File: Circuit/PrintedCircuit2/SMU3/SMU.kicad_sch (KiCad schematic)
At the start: 21 parts, among them J1 Conn_Coaxial, J2 Conn_Coaxial, SW1 SW_SPDT, SW2 SW_SPDT, U1 TPS65131_kit, U2 MCP1501-20xCH, U3 MCP4922

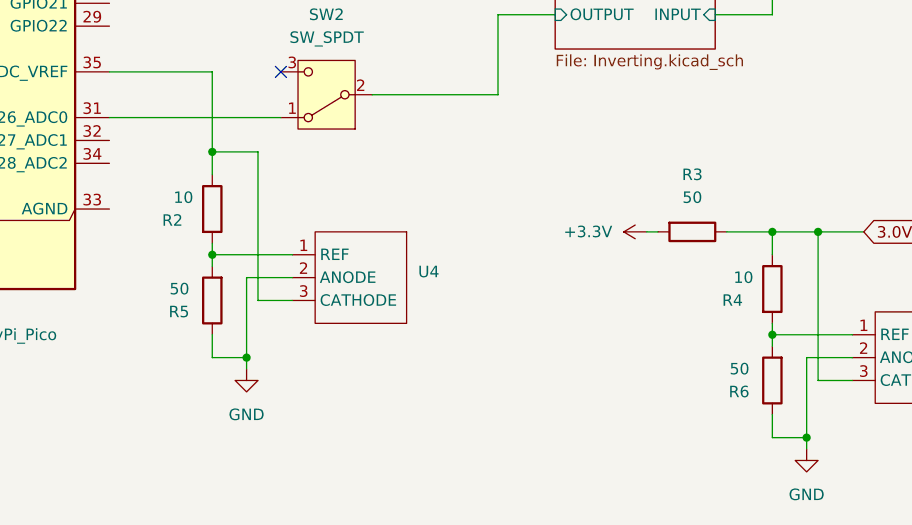
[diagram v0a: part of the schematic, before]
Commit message: 3Dモデルを更新
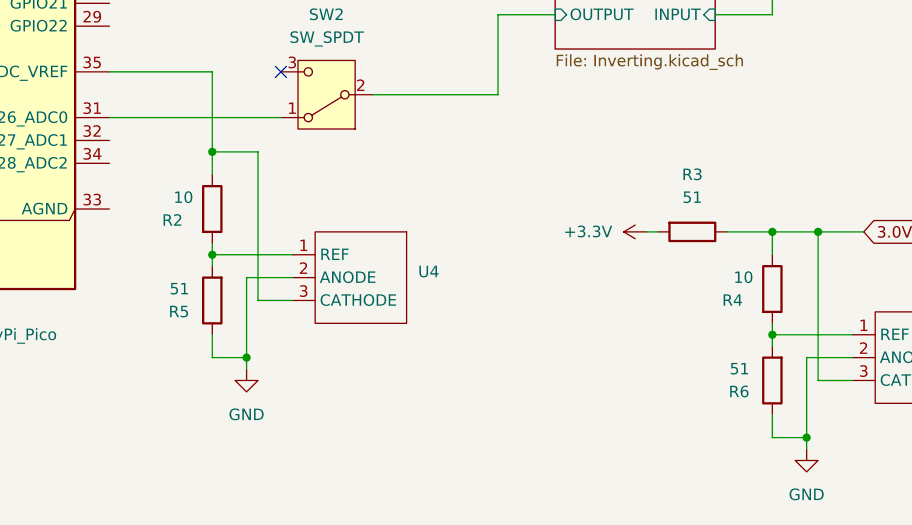
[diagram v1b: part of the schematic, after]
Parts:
- R3, R5, R6: value 50 -> 51
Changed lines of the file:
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@@
 			)
 		)
-		(property "Value" "50"
+		(property "Value" "51"
 			(at 83.82 153.6701 0)
 			(effects
@@
 			)
 		)
-		(property "Value" "50"
+		(property "Value" "51"
 			(at 139.7 143.51 90)
 			(effects
@@
 			)
 		)
-		(property "Value" "50"
+		(property "Value" "51"
 			(at 146.05 162.5601 0)
 			(effects

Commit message: 更新
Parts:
- R3, R6: value 51 -> 51Ω
- R4: value 10 -> 10Ω
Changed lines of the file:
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@@
 			)
 		)
-		(property "Value" "51"
+		(property "Value" "51Ω"
 			(at 139.7 143.51 90)
 			(effects
@@
 		(on_board yes)
 		(dnp no)
-		(fields_autoplaced yes)
 		(property "Reference" "R6"
-			(at 146.05 165.1001 0)
-			(effects
-				(font
-					(size 1.27 1.27)
-				)
-				(justify left)
-			)
-		)
-		(property "Value" "51"
-			(at 146.05 162.5601 0)
-			(effects
-				(font
-					(size 1.27 1.27)
-				)
-				(justify left)
+			(at 142.494 162.306 0)
+			(effects
+				(font
+					(size 1.27 1.27)
+				)
+				(justify right)
+			)
+		)
+		(property "Value" "51Ω"
+			(at 142.494 164.846 0)
+			(effects
+				(font
+					(size 1.27 1.27)
+				)
+				(justify right)
 			)
 		)
@@
 			)
 		)
-		(property "Value" "10"
-			(at 144.272 152.4 0)
-			(effects
-				(font
+		(property "Value" "10Ω"
+			(at 142.748 152.4 0)
+			(effects
+				(font

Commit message: β0.0.3
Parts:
- added R6: 51, Resistor_SMD:R_0603_1608Metric, symbol Device:R
- R2: value 10 -> 1k; footprint Resistor_SMD:R_0603_1608Metric_Pad0.98x0.95mm_HandSolder -> Resistor_SMD:R_0603_1608Metric
- R3: value 51Ω -> 51; footprint Resistor_SMD:R_0603_1608Metric_Pad0.98x0.95mm_HandSolder -> Resistor_SMD:R_0603_1608Metric
- R4: value 10Ω -> 1k; footprint Resistor_SMD:R_0603_1608Metric_Pad0.98x0.95mm_HandSolder -> Resistor_SMD:R_0603_1608Metric
- R5: value 51 -> 5.1k; footprint Resistor_SMD:R_0603_1608Metric_Pad0.98x0.95mm_HandSolder -> Resistor_SMD:R_0603_1608Metric
- R7: renamed from R6; value 51Ω -> 5.1k; footprint Resistor_SMD:R_0603_1608Metric_Pad0.98x0.95mm_HandSolder -> Resistor_SMD:R_0603_1608Metric
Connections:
- net +3.3V: now also R6.2
- net at A1.35 (ADC_VREF), R2.1, U4.3 (CATHODE): now also R6.1
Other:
- note removed: "SHDNの接続ミス PCB未修正"
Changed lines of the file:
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@@
 		)
 	)
-	(text "SHDNの接続ミス\nPCB未修正"
-		(exclude_from_sim no)
-		(at 94.234 55.626 0)
-		(effects
-			(font
-				(size 1.27 1.27)
-			)
-		)
+	(junction
+		(at 80.01 129.54)
+		(diameter 0)
+		(color 0 0 0 0)
 	)
 	(junction
@@
 	(wire
 		(pts
+			(xy 80.01 158.75) (xy 80.01 129.54)
+		)
+		(stroke
+			(width 0)
+			(type default)
+		)
+	)
+	(wire
+		(pts
 			(xy 223.52 113.03) (xy 231.14 113.03)
 		)
@@
 	(wire
 		(pts
-			(xy 74.93 129.54) (xy 86.36 129.54)
+			(xy 74.93 129.54) (xy 80.01 129.54)
 		)
 		(stroke
@@
 	(wire
 		(pts
+			(xy 80.01 167.64) (xy 80.01 166.37)
+		)
+		(stroke
+			(width 0)
+			(type default)
+		)
+	)
+	(wire
+		(pts
+			(xy 80.01 129.54) (xy 86.36 129.54)
+		)
+		(stroke
+			(width 0)
+			(type default)
+		)
+	)
+	(wire
+		(pts
 			(xy 190.5 104.14) (xy 200.66 104.14)
 		)
@@
 		(dnp no)
 		(fields_autoplaced yes)
-		(property "Reference" "#PWR015"
+		(property "Reference" "#PWR016"
 			(at 152.4 177.8 0)
 			(effects
@@
 			(project "SMU"
 				(path "/736408a4-d995-4f38-bf98-0d13d4319ec4"
-					(reference "#PWR015")
+					(reference "#PWR016")
 					(unit 1)
 				)
@@
 	)
 	(symbol
+		(lib_id "power:+3.3V")
+		(at 80.01 167.64 180)
+		(unit 1)
+		(exclude_from_sim no)
+		(in_bom yes)
+		(on_board yes)
+		(dnp no)
+		(fields_autoplaced yes)
+		(property "Reference" "#PWR015"
+			(at 80.01 163.83 0)
+			(effects
+				(font
+					(size 1.27 1.27)
+				)
+				(hide yes)
+			)
+		)
+		(property "Value" "+3.3V"
+			(at 80.0099 171.45 90)
+			(effects
+				(font
+					(size 1.27 1.27)
+				)
+				(justify left)
+			)
+		)
+		(property "Footprint" ""
+			(at 80.01 167.64 0)
+			(effects
+				(font
+					(size 1.27 1.27)
+				)
+				(hide yes)
+			)
+		)
+		(property "Datasheet" ""
+			(at 80.01 167.64 0)
+			(effects
+				(font
+					(size 1.27 1.27)
+				)
+				(hide yes)
+			)
+		)
+		(property "Description" "Power symbol creates a global label with name \"+3.3V\""
+			(at 80.01 167.64 0)
+			(effects
+				(font
+					(size 1.27 1.27)
+				)
+				(hide yes)
+			)
+		)
+		(pin "1"
+		)
+		(instances
+			(project "SMU"
+				(path "/736408a4-d995-4f38-bf98-0d13d4319ec4"
+					(reference "#PWR015")
+					(unit 1)
+				)
+			)
+		)
+	)
+	(symbol
 		(lib_id "power:-12V")
 		(at 80.01 41.91 270)
@@
 			)
 		)
-		(property "Value" "51"
+		(property "Value" "5.1k"
 			(at 83.82 153.6701 0)
 			(effects
@@
 			)
 		)
-		(property "Footprint" "Resistor_SMD:R_0603_1608Metric_Pad0.98x0.95mm_HandSolder"
+		(property "Footprint" "Resistor_SMD:R_0603_1608Metric"
 			(at 88.138 154.94 90)
 			(effects
@@
 			)
 		)
-		(property "Value" "51Ω"
+		(property "Value" "51"
 			(at 139.7 143.51 90)
 			(effects
@@
 			)
 		)
-		(property "Footprint" "Resistor_SMD:R_0603_1608Metric_Pad0.98x0.95mm_HandSolder"
+		(property "Footprint" "Resistor_SMD:R_0603_1608Metric"
 			(at 139.7 145.542 90)
 			(effects
@@
 			)
 		)
-		(property "Value" "10"
+		(property "Value" "1k"
 			(at 82.042 143.51 0)
 			(effects
@@
 			)
 		)
-		(property "Footprint" "Resistor_SMD:R_0603_1608Metric_Pad0.98x0.95mm_HandSolder"
+		(property "Footprint" "Resistor_SMD:R_0603_1608Metric"
 			(at 84.582 144.78 90)
 			(effects
@@
 	)
 	(symbol
+		(lib_id "Device:R")
+		(at 80.01 162.56 0)
+		(unit 1)
+		(exclude_from_sim no)
+		(in_bom yes)
+		(on_board yes)
+		(dnp no)
+		(fields_autoplaced yes)
+		(property "Reference" "R6"
+			(at 73.66 162.56 90)
+			(effects
+				(font
+					(size 1.27 1.27)
+				)
+			)
+		)
+		(property "Value" "51"
+			(at 76.2 162.56 90)
+			(effects
+				(font
+					(size 1.27 1.27)
+				)
+			)
+		)
+		(property "Footprint" "Resistor_SMD:R_0603_1608Metric"
+			(at 78.232 162.56 90)
+			(effects
+				(font
+					(size 1.27 1.27)
+				)
+				(hide yes)
+			)
+		)
+		(property "Datasheet" "~"
+			(at 80.01 162.56 0)
+			(effects
+				(font
+					(size 1.27 1.27)
+				)
+				(hide yes)
+			)
+		)
+		(property "Description" "Resistor"
+			(at 80.01 162.56 0)
+			(effects
+				(font
+					(size 1.27 1.27)
+				)
+				(hide yes)
+			)
+		)
+		(property "Sim.Device" "R"
+			(at 80.01 162.56 0)
+			(effects
+				(font
+					(size 1.27 1.27)
+				)
+				(hide yes)
+			)
+		)
+		(property "Sim.Type" "="
+			(at 80.01 162.56 0)
+			(effects
+				(font
+					(size 1.27 1.27)
+				)
+				(hide yes)
+			)
+		)
+		(property "Sim.Params" "r=30k"
+			(at 80.01 162.56 0)
+			(effects
+				(font
+					(size 1.27 1.27)
+				)
+				(hide yes)
+			)
+		)
+		(property "Sim.Pins" "1=+ 2=-"
+			(at 80.01 162.56 0)
+			(effects
+				(font
+					(size 1.27 1.27)
+				)
+				(hide yes)
+			)
+		)
+		(pin "2"
+		)
+		(pin "1"
+		)
+		(instances
+			(project "SMU"
+				(path "/736408a4-d995-4f38-bf98-0d13d4319ec4"
+					(reference "R6")
+					(unit 1)
+				)
+			)
+		)
+	)
+	(symbol
 		(lib_id "power:GND")
 		(at 111.76 62.23 0)
@@
 		(on_board yes)
 		(dnp no)
-		(property "Reference" "R6"
+		(property "Reference" "R7"
 			(at 142.494 162.306 0)
 			(effects
@@
 			)
 		)
-		(property "Value" "51Ω"
+		(property "Value" "5.1k"
 			(at 142.494 164.846 0)
 			(effects
@@
 			)
 		)
-		(property "Footprint" "Resistor_SMD:R_0603_1608Metric_Pad0.98x0.95mm_HandSolder"
+		(property "Footprint" "Resistor_SMD:R_0603_1608Metric"
 			(at 150.368 163.83 90)
 			(effects
@@
 			(project "SMU"
 				(path "/736408a4-d995-4f38-bf98-0d13d4319ec4"
-					(reference "R6")
+					(reference "R7")
 					(unit 1)
 				)
@@
 			)
 		)
-		(property "Value" "10Ω"
+		(property "Value" "1k"
 			(at 142.748 152.4 0)
 			(effects
@@
 			)
 		)
-		(property "Footprint" "Resistor_SMD:R_0603_1608Metric_Pad0.98x0.95mm_HandSolder"
+		(property "Footprint" "Resistor_SMD:R_0603_1608Metric"
 			(at 146.812 153.67 90)
 			(effects

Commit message: 保護回路を変更
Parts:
- renumbered C5 to C4, C4 to C5, R6 to R1, R5 to R3, R1 to R4, R3 to R5, R4 to R6, SW2 to SW1, SW1 to SW2, U4 to U2, U2 to U3, U3 to U4
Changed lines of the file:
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@@
 		(dnp no)
 		(fields_autoplaced yes)
-		(property "Reference" "#PWR09"
+		(property "Reference" "#PWR03"
 			(at 57.15 85.09 0)
 			(effects
@@
 			(project ""
 				(path "/736408a4-d995-4f38-bf98-0d13d4319ec4"
-					(reference "#PWR09")
+					(reference "#PWR03")
 					(unit 1)
 				)
@@
 		(dnp no)
 		(fields_autoplaced yes)
-		(property "Reference" "#PWR03"
+		(property "Reference" "#PWR09"
 			(at 99.06 26.67 0)
 			(effects
@@
 			(project "SMU"
 				(path "/736408a4-d995-4f38-bf98-0d13d4319ec4"
-					(reference "#PWR03")
+					(reference "#PWR09")
 					(unit 1)
 				)
@@
 		(dnp no)
 		(fields_autoplaced yes)
-		(property "Reference" "#PWR014"
+		(property "Reference" "#PWR02"
 			(at 52.07 171.45 0)
 			(effects
@@
 			(project ""
 				(path "/736408a4-d995-4f38-bf98-0d13d4319ec4"
-					(reference "#PWR014")
+					(reference "#PWR02")
 					(unit 1)
 				)
@@
 		(dnp no)
 		(fields_autoplaced yes)
-		(property "Reference" "#PWR010"
+		(property "Reference" "#PWR014"
 			(at 118.11 101.6 0)
 			(effects
@@
 			(project "SMU"
 				(path "/736408a4-d995-4f38-bf98-0d13d4319ec4"
-					(reference "#PWR010")
+					(reference "#PWR014")
 					(unit 1)
 				)
@@
 		(dnp no)
 		(fields_autoplaced yes)
-		(property "Reference" "SW2"
+		(property "Reference" "SW1"
 			(at 99.06 123.19 0)
 			(effects
@@
 			(project "SMU"
 				(path "/736408a4-d995-4f38-bf98-0d13d4319ec4"
-					(reference "SW2")
+					(reference "SW1")
 					(unit 1)
 				)
@@
 		(dnp no)
 		(fields_autoplaced yes)
-		(property "Reference" "#PWR012"
+		(property "Reference" "#PWR015"
 			(at 138.43 147.32 0)
 			(effects
@@
 			(project "SMU"
 				(path "/736408a4-d995-4f38-bf98-0d13d4319ec4"
-					(reference "#PWR012")
+					(reference "#PWR015")
 					(unit 1)
 				)
@@
 		(dnp no)
 		(fields_autoplaced yes)
-		(property "Reference" "#PWR01"
+		(property "Reference" "#PWR07"
 			(at 77.47 21.59 0)
 			(effects
@@
 			(project ""
 				(path "/736408a4-d995-4f38-bf98-0d13d4319ec4"
-					(reference "#PWR01")
+					(reference "#PWR07")
 					(unit 1)
 				)
@@
 		(dnp no)
 		(fields_autoplaced yes)
-		(property "Reference" "C5"
+		(property "Reference" "C4"
 			(at 107.95 109.2199 0)
 			(effects
@@
 			(project "SMU"
 				(path "/736408a4-d995-4f38-bf98-0d13d4319ec4"
-					(reference "C5")
+					(reference "C4")
 					(unit 1)
 				)
@@
 		(on_board yes)
 		(dnp no)
-		(property "Reference" "R1"
+		(property "Reference" "R4"
 			(at 128.27 64.77 90)
 			(effects
@@
 			(project ""
 				(path "/736408a4-d995-4f38-bf98-0d13d4319ec4"
-					(reference "R1")
+					(reference "R4")
 					(unit 1)
 				)
@@
 		(dnp no)
 		(fields_autoplaced yes)
-		(property "Reference" "U2"
+		(property "Reference" "U3"
 			(at 129.54 45.7514 0)
 			(effects
@@
 			(project ""
 				(path "/736408a4-d995-4f38-bf98-0d13d4319ec4"
-					(reference "U2")
+					(reference "U3")
 					(unit 1)
 				)
@@
 		(dnp no)
 		(fields_autoplaced yes)
-		(property "Reference" "SW1"
+		(property "Reference" "SW2"
 			(at 208.28 91.44 0)
 			(effects
@@
 			(project "SMU"
 				(path "/736408a4-d995-4f38-bf98-0d13d4319ec4"
-					(reference "SW1")
+					(reference "SW2")
 					(unit 1)
 				)
@@
 		(on_board yes)
 		(dnp no)
-		(property "Reference" "C4"
+		(property "Reference" "C5"
 			(at 118.11 65.024 90)
 			(effects
@@
 			(project "SMU"
 				(path "/736408a4-d995-4f38-bf98-0d13d4319ec4"
-					(reference "C4")
+					(reference "C5")
 					(unit 1)
 				)
@@
 		(dnp no)
 		(fields_autoplaced yes)
-		(property "Reference" "#PWR015"
+		(property "Reference" "#PWR06"
 			(at 80.01 163.83 0)
 			(effects
@@
 			(project "SMU"
 				(path "/736408a4-d995-4f38-bf98-0d13d4319ec4"
-					(reference "#PWR015")
+					(reference "#PWR06")
 					(unit 1)
 				)
@@
 		(dnp no)
 		(fields_autoplaced yes)
-		(property "Reference" "#PWR06"
+		(property "Reference" "#PWR05"
 			(at 76.2 41.91 0)
 			(effects
@@
 			(project ""
 				(path "/736408a4-d995-4f38-bf98-0d13d4319ec4"
-					(reference "#PWR06")
+					(reference "#PWR05")
 					(unit 1)
 				)
@@
 		(dnp no)
 		(fields_autoplaced yes)
-		(property "Reference" "#PWR013"
+		(property "Reference" "#PWR08"
 			(at 90.17 168.91 0)
 			(effects
@@
 			(project "SMU"
 				(path "/736408a4-d995-4f38-bf98-0d13d4319ec4"
-					(reference "#PWR013")
+					(reference "#PWR08")
 					(unit 1)
 				)
@@
 		(dnp no)
 		(fields_autoplaced yes)
-		(property "Reference" "#PWR011"
+		(property "Reference" "#PWR010"
 			(at 104.14 121.92 0)
 			(effects
@@
 			(project "SMU"
 				(path "/736408a4-d995-4f38-bf98-0d13d4319ec4"
-					(reference "#PWR011")
+					(reference "#PWR010")
 					(unit 1)
 				)
@@
 		(dnp no)
 		(fields_autoplaced yes)
-		(property "Reference" "R5"
+		(property "Reference" "R3"
 			(at 83.82 156.2101 0)
 			(effects
@@
 			(project "SMU"
 				(path "/736408a4-d995-4f38-bf98-0d13d4319ec4"
-					(reference "R5")
+					(reference "R3")
 					(unit 1)
 				)
@@
 		(dnp no)
 		(fields_autoplaced yes)
-		(property "Reference" "R3"
+		(property "Reference" "R5"
 			(at 139.7 140.97 90)
 			(effects
@@
 			(project "SMU"
 				(path "/736408a4-d995-4f38-bf98-0d13d4319ec4"
-					(reference "R3")
+					(reference "R5")
 					(unit 1)
 				)
@@
 		(dnp no)
 		(fields_autoplaced yes)
-		(property "Reference" "#PWR04"
+		(property "Reference" "#PWR011"
 			(at 111.76 36.83 0)
 			(effects
@@
 			(project "SMU"
 				(path "/736408a4-d995-4f38-bf98-0d13d4319ec4"
-					(reference "#PWR04")
+					(reference "#PWR011")
 					(unit 1)
 				)
@@
 		(on_board yes)
 		(dnp no)
-		(property "Reference" "U3"
+		(property "Reference" "U4"
 			(at 120.3041 105.41 0)
 			(effects
@@
 			(project ""
 				(path "/736408a4-d995-4f38-bf98-0d13d4319ec4"
-					(reference "U3")
+					(reference "U4")
 					(unit 1)
 				)
@@
 		(dnp no)
 		(fields_autoplaced yes)
-		(property "Reference" "R6"
+		(property "Reference" "R1"
 			(at 73.66 162.56 90)
 			(effects
@@
 			(project "SMU"
 				(path "/736408a4-d995-4f38-bf98-0d13d4319ec4"
-					(reference "R6")
+					(reference "R1")
 					(unit 1)
 				)
@@
 		(dnp no)
 		(fields_autoplaced yes)
-		(property "Reference" "#PWR07"
+		(property "Reference" "#PWR012"
 			(at 111.76 68.58 0)
 			(effects
@@
 			(project "SMU"
 				(path "/736408a4-d995-4f38-bf98-0d13d4319ec4"
-					(reference "#PWR07")
+					(reference "#PWR012")
 					(unit 1)
 				)
@@
 		(dnp no)
 		(fields_autoplaced yes)
-		(property "Reference" "#PWR08"
+		(property "Reference" "#PWR013"
 			(at 118.11 71.12 0)
 			(effects
@@
 			(project "SMU"
 				(path "/736408a4-d995-4f38-bf98-0d13d4319ec4"
-					(reference "#PWR08")
+					(reference "#PWR013")
 					(unit 1)
 				)
@@
 		(dnp no)
 		(fields_autoplaced yes)
-		(property "Reference" "#PWR05"
+		(property "Reference" "#PWR01"
 			(at 35.56 35.56 0)
 			(effects
@@
 			(project "SMU"
 				(path "/736408a4-d995-4f38-bf98-0d13d4319ec4"
-					(reference "#PWR05")
+					(reference "#PWR01")
 					(unit 1)
 				)
@@
 		(dnp no)
 		(fields_autoplaced yes)
-		(property "Reference" "#PWR02"
+		(property "Reference" "#PWR04"
 			(at 86.36 31.75 0)
 			(effects
@@
 			(project "SMU"
 				(path "/736408a4-d995-4f38-bf98-0d13d4319ec4"
-					(reference "#PWR02")
+					(reference "#PWR04")
 					(unit 1)
 				)
@@
 		(dnp no)
 		(fields_autoplaced yes)
-		(property "Reference" "U4"
+		(property "Reference" "U2"
 			(at 109.22 151.7649 90)
 			(effects
@@
 			(project "SMU"
 				(path "/736408a4-d995-4f38-bf98-0d13d4319ec4"
-					(reference "U4")
+					(reference "U2")
 					(unit 1)
 				)
@@
 		(on_board yes)
 		(dnp no)
-		(property "Reference" "R4"
+		(property "Reference" "R6"
 			(at 143.002 154.94 0)
 			(effects
@@
 			(project "SMU"
 				(path "/736408a4-d995-4f38-bf98-0d13d4319ec4"
-					(reference "R4")
-					(unit 1)
-				)
+					(reference "R6")
+					(unit 1)
+				)
